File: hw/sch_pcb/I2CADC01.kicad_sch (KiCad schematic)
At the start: 33 parts

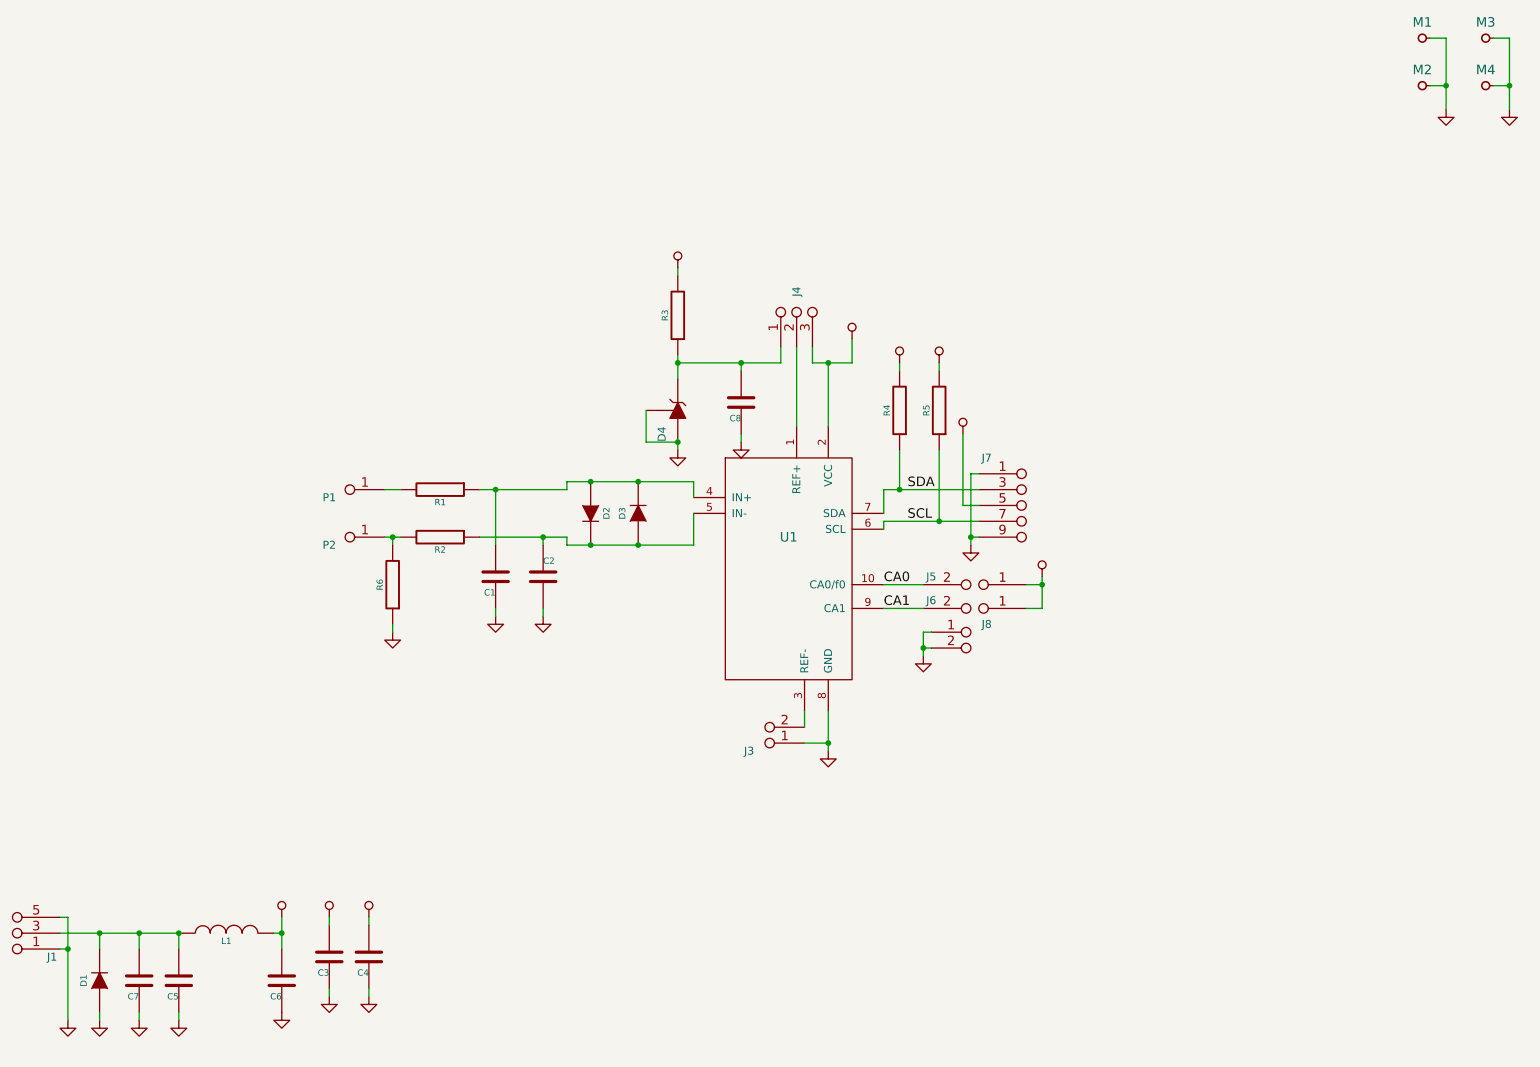
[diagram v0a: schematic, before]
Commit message: Adding assets update title block.
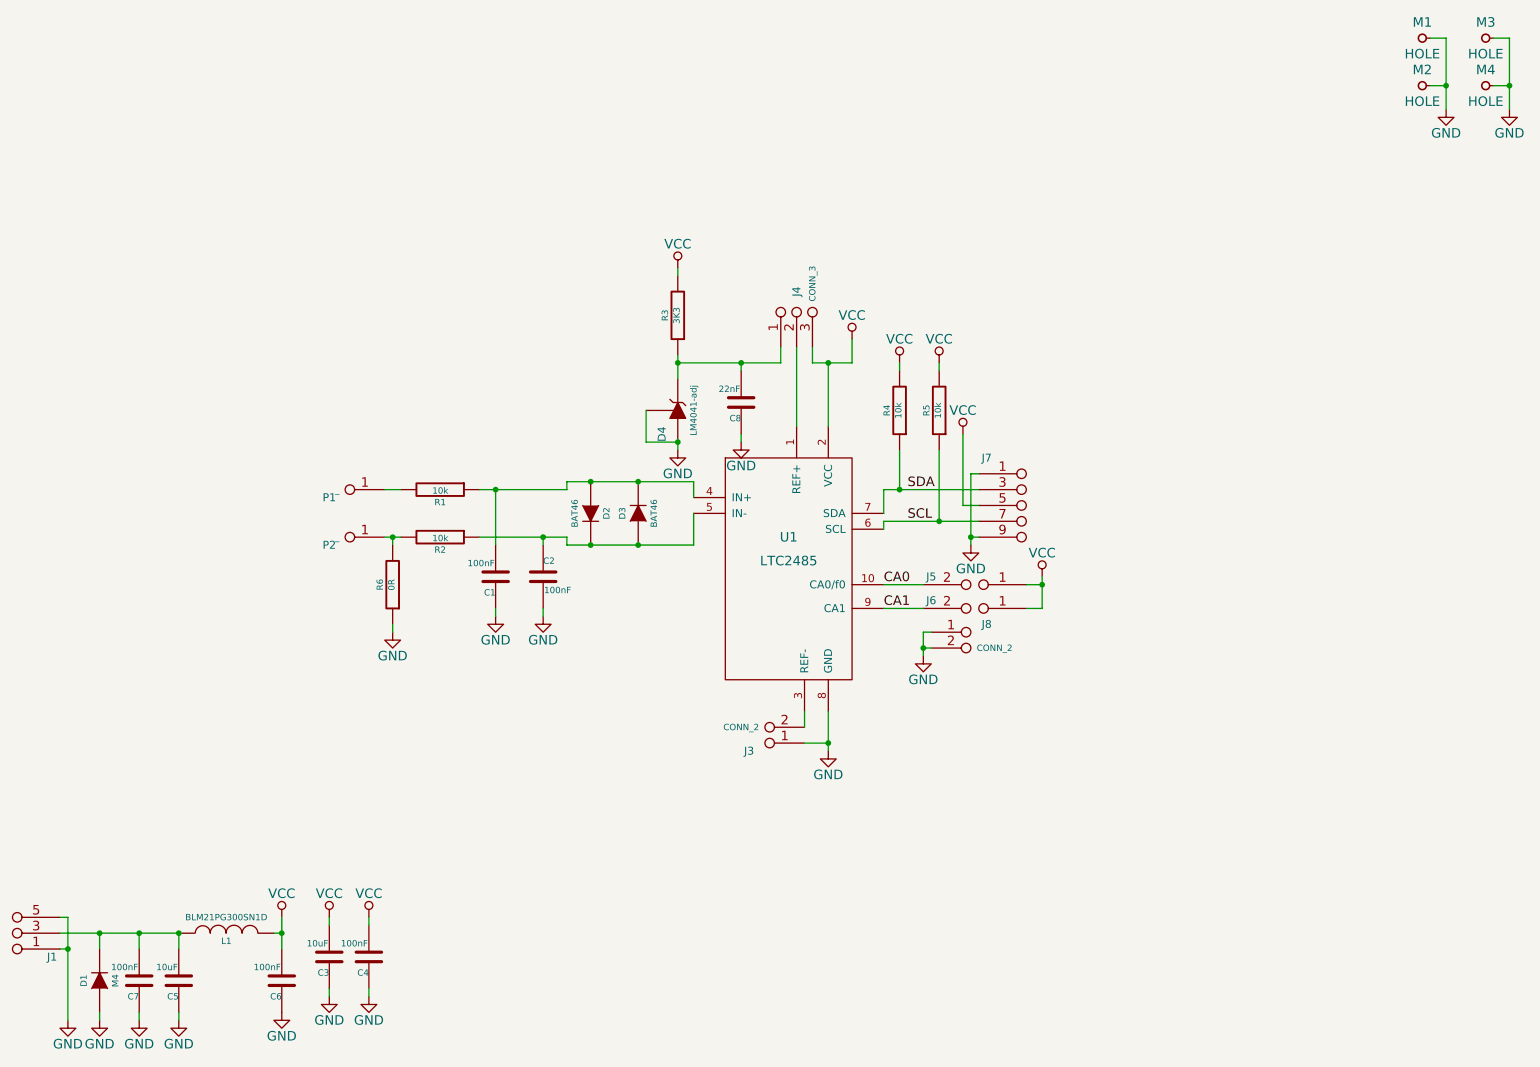
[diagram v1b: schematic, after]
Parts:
- C1, C2, C4, C6, C7: value (none) -> 100nF; footprint (none) -> Mlab_R:SMD-0805
- C3, C5: value (none) -> 10uF; footprint (none) -> Mlab_R:SMD-0805
- C8: value (none) -> 22nF; footprint (none) -> Mlab_R:SMD-0805
- D1: value (none) -> M4; footprint (none) -> Mlab_D:SMA_Standard
- D2, D3: value (none) -> BAT46; footprint (none) -> Mlab_D:MiniMELF_Standard
- D4: value (none) -> LM4041-adj; footprint (none) -> Mlab_IO:SOT-23
- J1: value (none) -> JUMP_3X2; footprint (none) -> Mlab_Pin_Headers:Straight_2x03
- J3, J8: value (none) -> CONN_2; footprint (none) -> Mlab_Pin_Headers:Straight_2x01
- J4: value (none) -> CONN_3; footprint (none) -> Mlab_Pin_Headers:Straight_1x03
- J5, J6: value (none) -> JUMP2_2x1; footprint (none) -> Mlab_Pin_Headers:Straight_2x01
- J7: value (none) -> JUMP_5X2; footprint (none) -> Mlab_Pin_Headers:Straight_2x05
- L1: value (none) -> BLM21PG300SN1D; footprint (none) -> Mlab_R:SMD-0805
- M1, M2, M3, M4: value (none) -> HOLE; footprint (none) -> Mlab_Mechanical:MountingHole_3mm
- P1, P2: value (none) -> _; footprint (none) -> Mlab_Con:WAGO256
- R1, R2, R4, R5: value (none) -> 10k; footprint (none) -> Mlab_R:SMD-0805
- R3: value (none) -> 3K3; footprint (none) -> Mlab_R:SMD-0805
- R6: value (none) -> 0R; footprint (none) -> Mlab_R:SMD-0805
- U1: value (none) -> LTC2485; footprint (none) -> Housings_DFN_QFN:DFN-10-1EP_3x3mm_Pitch0.5mm
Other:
- company: (none) -> mlab.cz
- title: (none) -> I2CADC01

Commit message: Update project files. cleanup repository.
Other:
- title: I2CADC01 -> I2CADC01A
- moved on the sheet: C8, D4, J7, R3, R4, R5
